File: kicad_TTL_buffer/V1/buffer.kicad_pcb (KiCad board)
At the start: 2 copper layers, 54.4 x 23.2 mm, 19 parts, among them P1 Conn_02x06_Odd_Even, P2 Conn_01x04, P3 Conn_01x06, P4 Conn_01x03_ODD, P5 Conn_01x03_EVEN, P6 Conn_01x01, P7 Conn_01x01, U1 74LS08

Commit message: Update TTL buffer
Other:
- board text added: "TTL buffer/adapter for RGBtoHD"
- board text removed: "TTL buffer/adaptor for RGBtoHD"
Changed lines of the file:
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@@
   (gr_line (start 42.462 44.56176) (end 42.462 34.30016) (layer B.SilkS) (width 0.15))
   (gr_line (start 41.6492 44.56176) (end 42.462 44.56176) (layer B.SilkS) (width 0.15))
-  (gr_text "TTL buffer/adaptor for RGBtoHD" (at 54.5778 51.66106) (layer B.SilkS)
+  (gr_text "TTL buffer/adapter for RGBtoHD" (at 54.5778 51.66106) (layer B.SilkS)
     (effects (font (size 0.8 0.8) (thickness 0.12)) (justify mirror))
   )

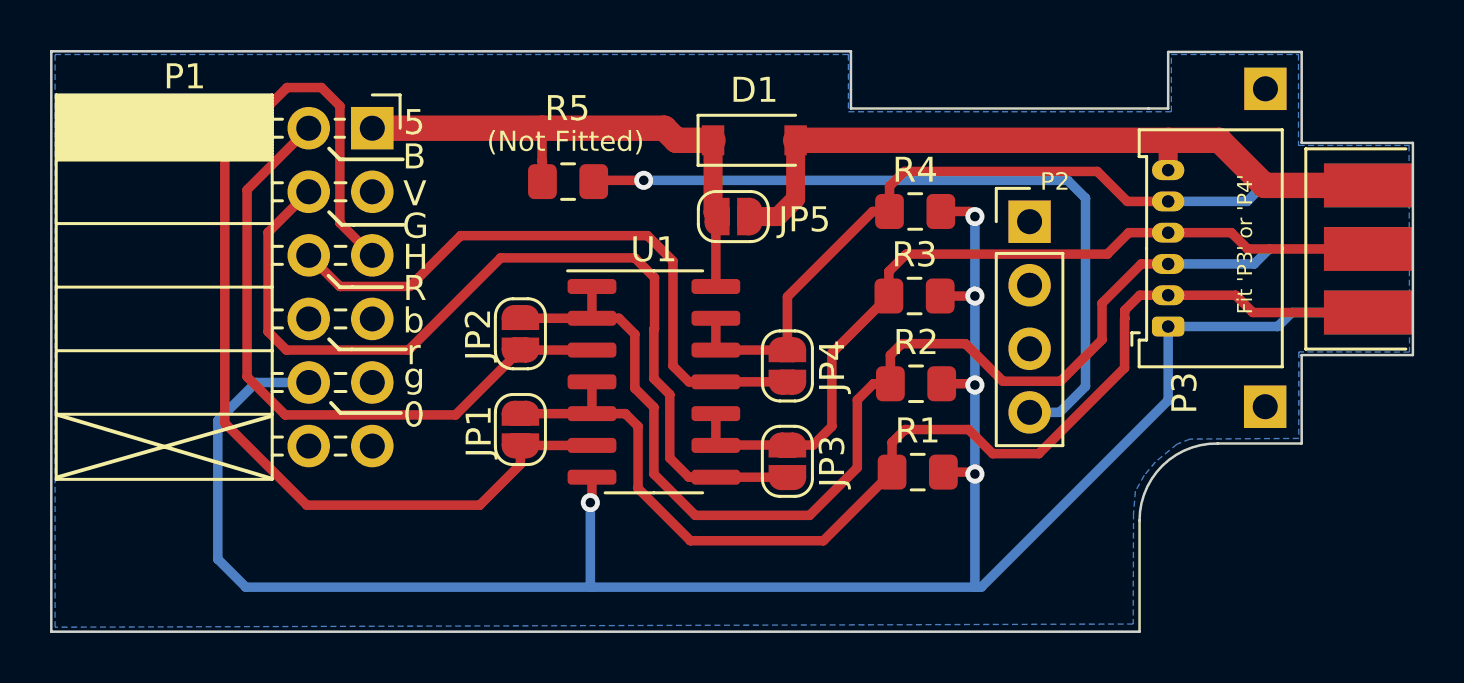
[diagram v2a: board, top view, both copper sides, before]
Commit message: Update TTL V1 board
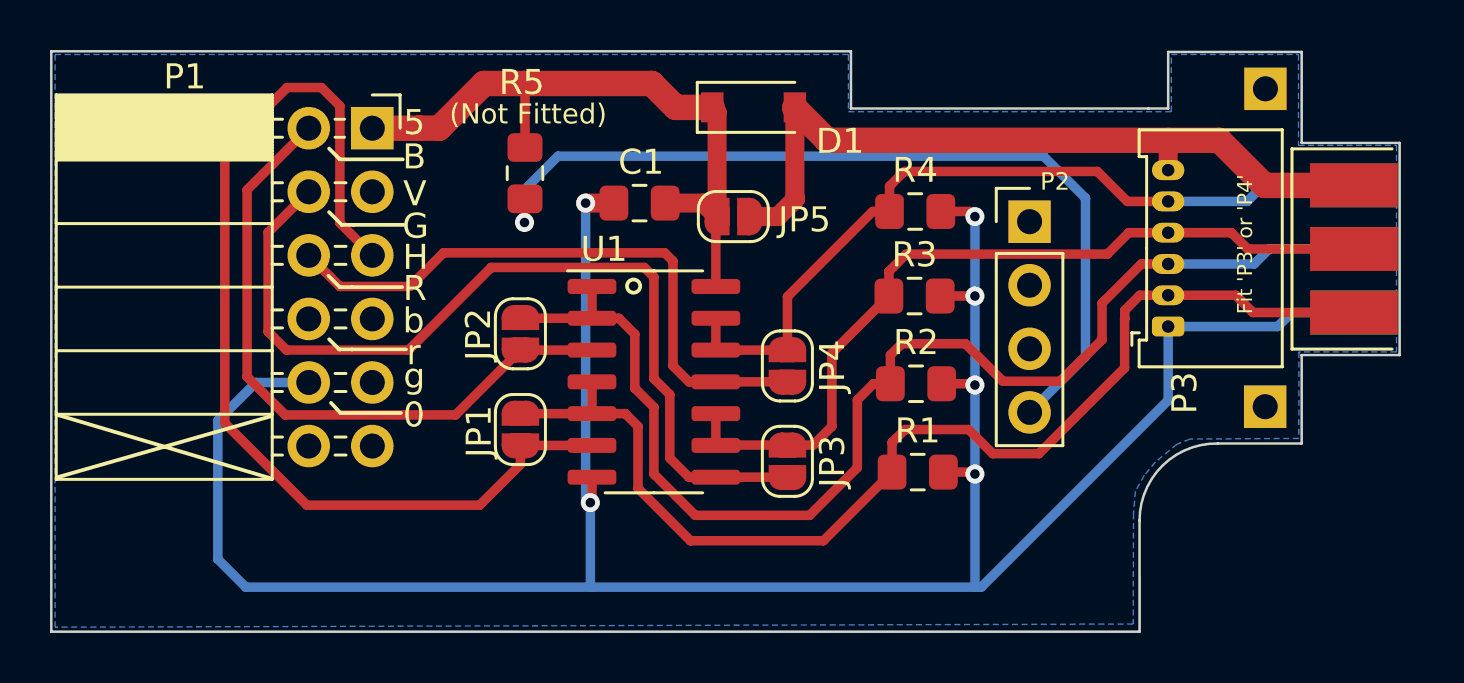
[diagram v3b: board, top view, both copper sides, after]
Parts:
- added C1: 100n, Capacitor_SMD:C_0805_2012Metric_Pad1.15x1.40mm_HandSolder, F.Cu at (51.0, 37.4)
- moved R5 1.75 mm to (46.5, 36.2), turned to 270 degrees
- moved D1 1.32 mm to (55.6, 33.5)
- moved P4 0.55 mm to (85.1, 39.2)
- moved P5 0.55 mm to (85.1, 39.2)
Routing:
- net /GND: track 87.4 -> 100.0 mm, vias 5 -> 6
- net Net-(P2-Pad4): track 30.2 -> 35.6 mm
- net /VCC: track 21.9 -> 27.1 mm
- net /VCC_IN: track 29.3 -> 30.6 mm
- net /RED: track 25.5 -> 24.9 mm
- net /ASYNC: track 46.1 -> 45.5 mm
- net /ARED: track 32.9 -> 32.4 mm
- net /AGREEN: track 33.4 -> 32.9 mm
- net /ABLUE: track 50.0 -> 49.4 mm
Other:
- board size 54.4 x 23.2 mm -> 53.9 x 23.2 mm

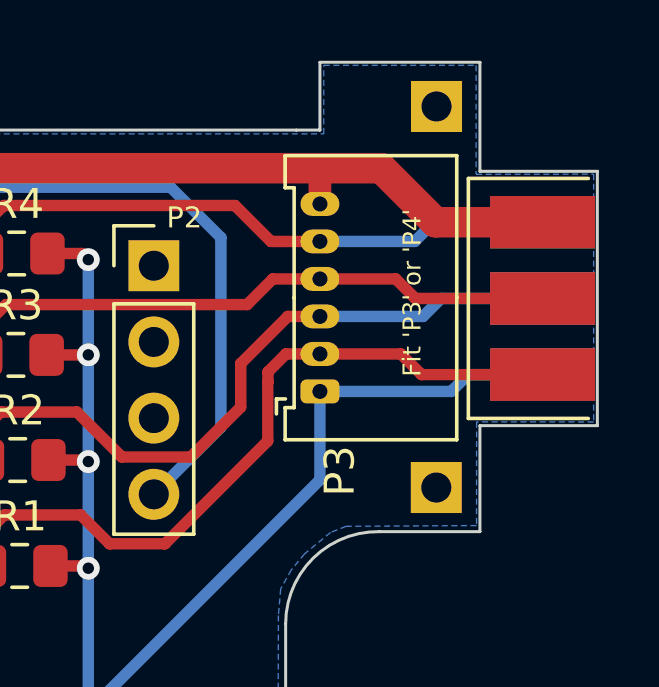
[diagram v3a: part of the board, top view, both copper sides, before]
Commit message: Extend P4 pads on TTL board
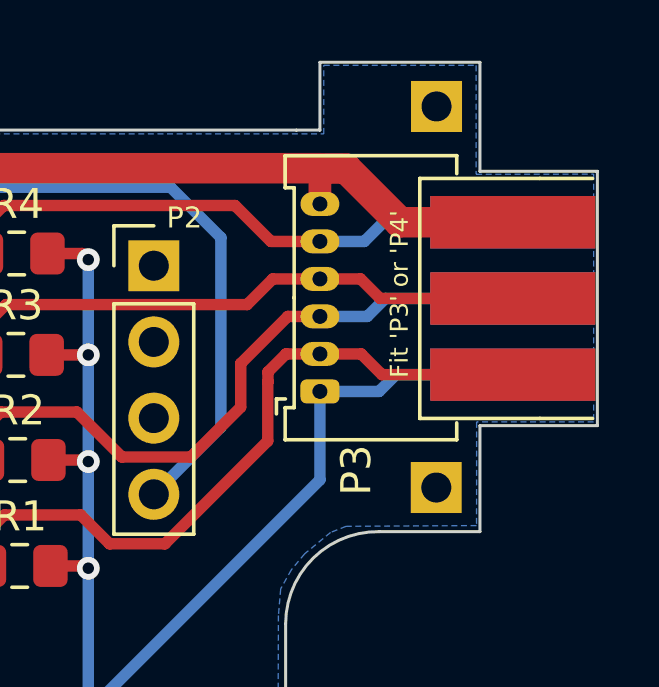
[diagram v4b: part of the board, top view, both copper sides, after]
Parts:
- P3: footprint Connector_Molex:Molex_PicoBlade_53048-0610_1x06_P1.25mm_Horizontal -> Connector_Molex:Molex_PicoBlade_53048-0610_1x06_P1.25mm_Horizontal_Custom2
- P4: footprint Connector_Harwin:Harwin_M20-89003xx_1x03_P2.54mm_Horizontal_Custom_ODD -> Connector_Harwin:Harwin_M20-89003xx_1x03_P2.54mm_Horizontal_Custom_ODD2
- P5: footprint Connector_Harwin:Harwin_M20-89003xx_1x03_P2.54mm_Horizontal_Custom_EVEN -> Connector_Harwin:Harwin_M20-89003xx_1x03_P2.54mm_Horizontal_Custom_EVEN2
- moved P4 1.62 mm to (83.5, 39.2)
- moved P5 1.62 mm to (83.5, 39.2)
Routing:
- net /AGREEN: track 32.9 -> 31.9 mm
- net /GND: track 100.0 -> 99.0 mm
- net /ASYNC: track 45.5 -> 44.5 mm
- net /ARED: track 32.4 -> 31.4 mm
- net /ABLUE: track 49.4 -> 48.4 mm
- net /VCC_IN: track 30.6 -> 29.7 mm
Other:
- board text added: "Pin1"
- board text removed: "Pin 1"
